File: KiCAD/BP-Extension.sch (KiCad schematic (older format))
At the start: 8 parts, among them P1 CONN_01X06, P2 CONN_01X01, SW1 SW_Push, U1 BP, U2 RFM69

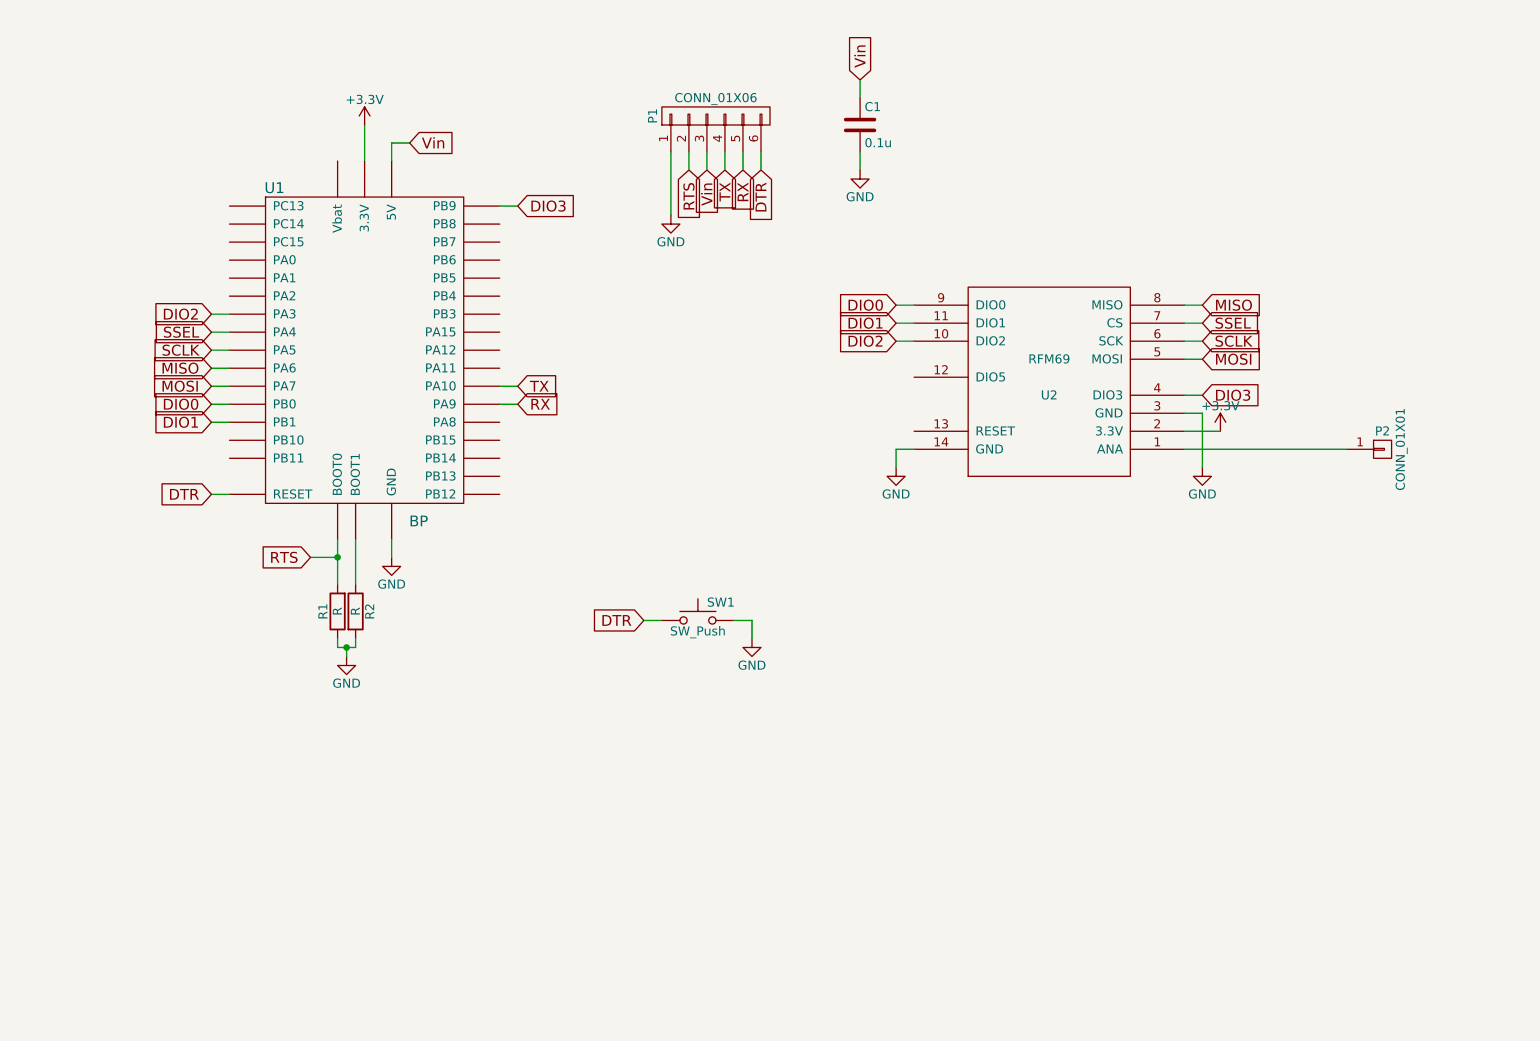
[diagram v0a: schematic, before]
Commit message: Moved 2x03 header to get rid of the offset, #8
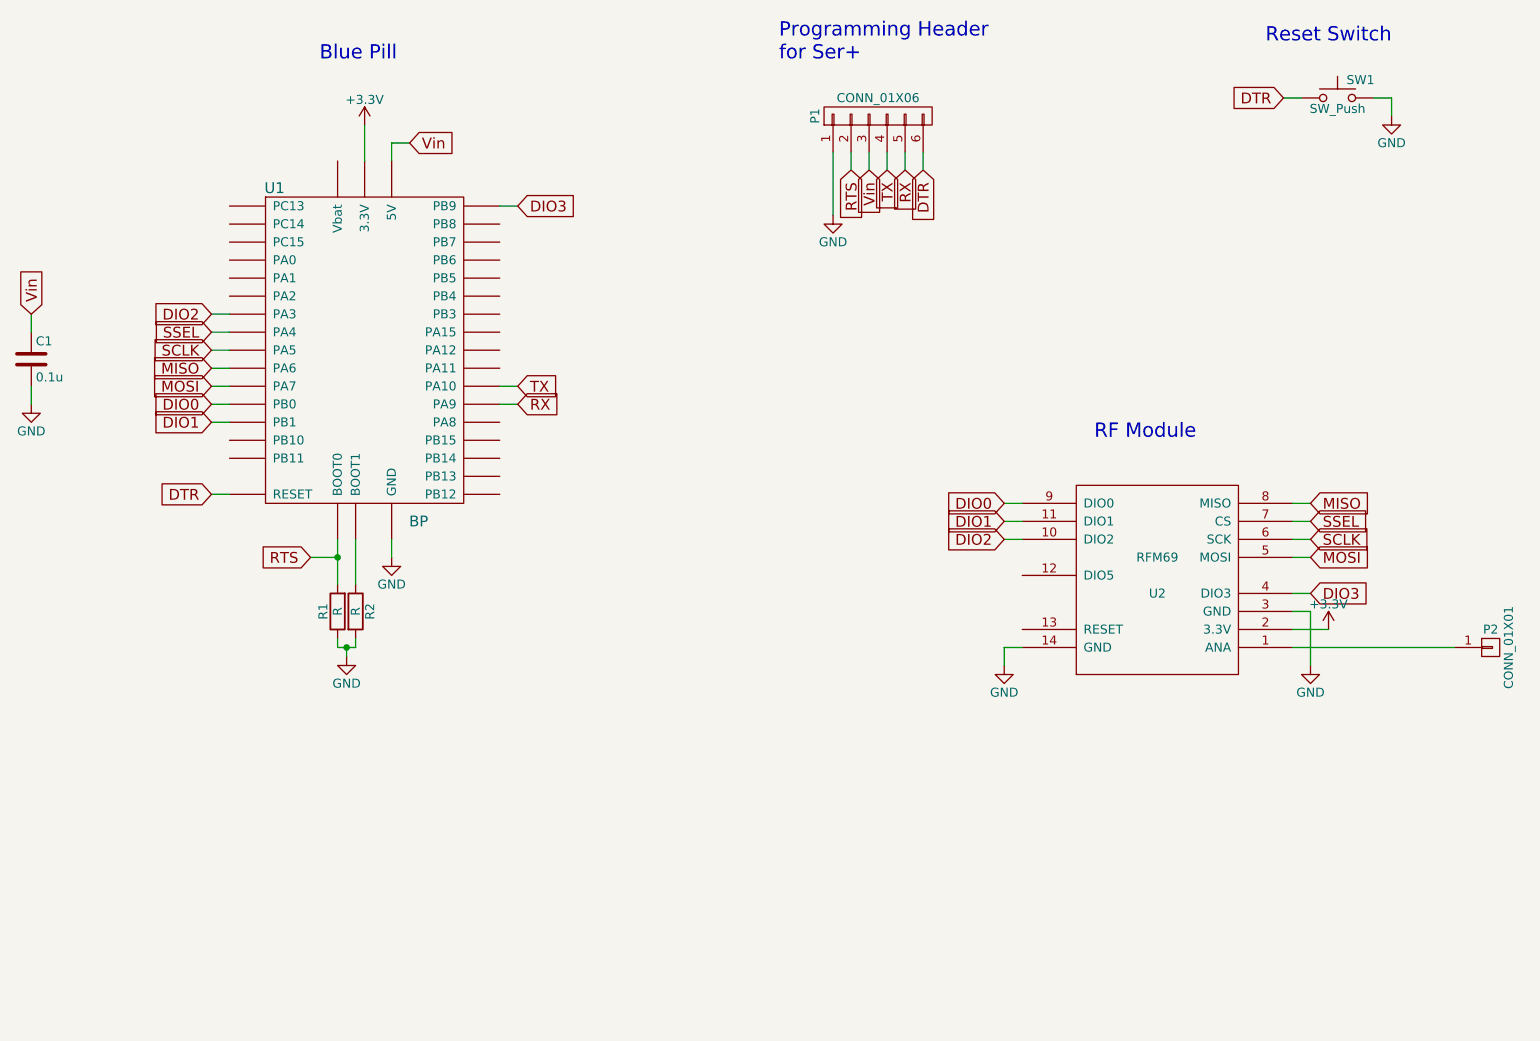
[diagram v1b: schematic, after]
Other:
- note added: "Blue Pill"
- note added: "Programming Header\nfor Ser+"
- note added: "RF Module"
- note added: "Reset Switch"
- moved on the sheet: C1, P1, P2, SW1, U2
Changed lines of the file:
@@
 LIBS:rfm69
 LIBS:switches
-LIBS:mechanical
 LIBS:BP-Extension-cache
 EELAYER 25 0
@@
 L CONN_01X06 P1
 U 1 1 58713DA3
-P 5200 2000
-F 0 "P1" H 5200 2350 50  0000 C CNN
-F 1 "CONN_01X06" V 5300 2000 50  0000 C CNN
-F 2 "Pin_Headers:Pin_Header_Angled_1x06_Pitch2.54mm" H 5200 2000 50  0001 C CNN
-F 3 "" H 5200 2000 50  0000 C CNN
-	1    5200 2000
+P 6100 2000
+F 0 "P1" H 6100 2350 50  0000 C CNN
+F 1 "CONN_01X06" V 6200 2000 50  0000 C CNN
+F 2 "Pin_Headers:Pin_Header_Angled_1x06_Pitch2.54mm" H 6100 2000 50  0001 C CNN
+F 3 "" H 6100 2000 50  0000 C CNN
+	1    6100 2000
 	0    -1   -1   0
 $EndComp
@@
 L GND #PWR04
 U 1 1 58713F1E
-P 4950 2550
-F 0 "#PWR04" H 4950 2300 50  0001 C CNN
-F 1 "GND" H 4950 2400 50  0000 C CNN
-F 2 "" H 4950 2550 50  0000 C CNN
-F 3 "" H 4950 2550 50  0000 C CNN
-	1    4950 2550
-	1    0    0    -1
-$EndComp
-Text GLabel 5050 2300 3    60   Input ~ 0
+P 5850 2550
+F 0 "#PWR04" H 5850 2300 50  0001 C CNN
+F 1 "GND" H 5850 2400 50  0000 C CNN
+F 2 "" H 5850 2550 50  0000 C CNN
+F 3 "" H 5850 2550 50  0000 C CNN
+	1    5850 2550
+	1    0    0    -1
+$EndComp
+Text GLabel 5950 2300 3    60   Input ~ 0
 RTS
-Text GLabel 5250 2300 3    60   Input ~ 0
+Text GLabel 6150 2300 3    60   Input ~ 0
 TX
-Text GLabel 5350 2300 3    60   Input ~ 0
+Text GLabel 6250 2300 3    60   Input ~ 0
 RX
-Text GLabel 5450 2300 3    60   Input ~ 0
+Text GLabel 6350 2300 3    60   Input ~ 0
 DTR
 Text GLabel 2400 4100 0    60   Input ~ 0
@@
 TX
 Wire Wire Line
-	5450 2200 5450 2300
+	6350 2200 6350 2300
 Wire Wire Line
 	2400 4100 2500 4100
@@
 	4000 3600 4100 3600
 Wire Wire Line
-	5250 2300 5250 2200
-Wire Wire Line
-	5350 2200 5350 2300
-Wire Wire Line
-	4950 2200 4950 2550
-Wire Wire Line
-	5050 2200 5050 2300
+	6150 2300 6150 2200
+Wire Wire Line
+	6250 2200 6250 2300
+Wire Wire Line
+	5850 2200 5850 2550
+Wire Wire Line
+	5950 2200 5950 2300
 Text GLabel 2950 4450 0    60   Input ~ 0
 RTS
@@
 	2950 4450 3100 4450
 Connection ~ 3100 4450
-Text GLabel 5150 2300 3    60   Input ~ 0
+Text GLabel 6050 2300 3    60   Input ~ 0
 Vin
 Wire Wire Line
-	5150 2200 5150 2300
+	6050 2200 6050 2300
 Text GLabel 3500 2150 2    60   Input ~ 0
 Vin
@@
 L RFM69 U2
 U 1 1 58716C00
-P 7050 3450
-F 0 "U2" H 7050 3350 50  0000 C CNN
-F 1 "RFM69" H 7050 3550 50  0000 C CNN
-F 2 "RFM69:RFM69CW" H 7050 3050 50  0001 C CNN
-F 3 "DOCUMENTATION" H 7100 2950 50  0001 C CNN
-	1    7050 3450
+P 7650 4550
+F 0 "U2" H 7650 4450 50  0000 C CNN
+F 1 "RFM69" H 7650 4650 50  0000 C CNN
+F 2 "RFM69:RFM69CW" H 7650 4150 50  0001 C CNN
+F 3 "DOCUMENTATION" H 7700 4050 50  0001 C CNN
+	1    7650 4550
 	1    0    0    -1
 $EndComp
@@
 L GND #PWR05
 U 1 1 58716C60
-P 7900 3950
-F 0 "#PWR05" H 7900 3700 50  0001 C CNN
-F 1 "GND" H 7900 3800 50  0000 C CNN
-F 2 "" H 7900 3950 50  0000 C CNN
-F 3 "" H 7900 3950 50  0000 C CNN
-	1    7900 3950
+P 8500 5050
+F 0 "#PWR05" H 8500 4800 50  0001 C CNN
+F 1 "GND" H 8500 4900 50  0000 C CNN
+F 2 "" H 8500 5050 50  0000 C CNN
+F 3 "" H 8500 5050 50  0000 C CNN
+	1    8500 5050
 	1    0    0    -1
 $EndComp
@@
 L +3.3V #PWR06
 U 1 1 58716C96
-P 8000 3750
-F 0 "#PWR06" H 8000 3600 50  0001 C CNN
-F 1 "+3.3V" H 8000 3890 50  0000 C CNN
-F 2 "" H 8000 3750 50  0000 C CNN
-F 3 "" H 8000 3750 50  0000 C CNN
-	1    8000 3750
-	1    0    0    -1
-$EndComp
-Text GLabel 7900 3150 2    60   Input ~ 0
+P 8600 4850
+F 0 "#PWR06" H 8600 4700 50  0001 C CNN
+F 1 "+3.3V" H 8600 4990 50  0000 C CNN
+F 2 "" H 8600 4850 50  0000 C CNN
+F 3 "" H 8600 4850 50  0000 C CNN
+	1    8600 4850
+	1    0    0    -1
+$EndComp
+Text GLabel 8500 4250 2    60   Input ~ 0
 SSEL
-Text GLabel 7900 3250 2    60   Input ~ 0
+Text GLabel 8500 4350 2    60   Input ~ 0
 SCLK
-Text GLabel 7900 3050 2    60   Input ~ 0
+Text GLabel 8500 4150 2    60   Input ~ 0
 MISO
-Text GLabel 7900 3350 2    60   Input ~ 0
+Text GLabel 8500 4450 2    60   Input ~ 0
 MOSI
 $Comp
 L CONN_01X01 P2
 U 1 1 58716DE4
-P 8900 3850
-F 0 "P2" H 8900 3950 50  0000 C CNN
-F 1 "CONN_01X01" V 9000 3850 50  0000 C CNN
-F 2 "Connect:PINTST" H 8900 3850 50  0001 C CNN
-F 3 "" H 8900 3850 50  0000 C CNN
-	1    8900 3850
-	1    0    0    -1
-$EndComp
-Wire Wire Line
-	7800 3650 7900 3650
-Wire Wire Line
-	7900 3650 7900 3950
+P 9500 4950
+F 0 "P2" H 9500 5050 50  0000 C CNN
+F 1 "CONN_01X01" V 9600 4950 50  0000 C CNN
+F 2 "Connect:PINTST" H 9500 4950 50  0001 C CNN
+F 3 "" H 9500 4950 50  0000 C CNN
+	1    9500 4950
+	1    0    0    -1
+$EndComp
+Wire Wire Line
+	8400 4750 8500 4750
+Wire Wire Line
+	8500 4750 8500 5050
 $Comp
 L GND #PWR07
 U 1 1 58717D5A
-P 6200 3950
-F 0 "#PWR07" H 6200 3700 50  0001 C CNN
-F 1 "GND" H 6200 3800 50  0000 C CNN
-F 2 "" H 6200 3950 50  0000 C CNN
-F 3 "" H 6200 3950 50  0000 C CNN
-	1    6200 3950
-	1    0    0    -1
-$EndComp
-Wire Wire Line
-	6300 3850 6200 3850
-Wire Wire Line
-	6200 3850 6200 3950
-Wire Wire Line
-	7800 3750 8000 3750
-Wire Wire Line
-	7800 3050 7900 3050
-Wire Wire Line
-	7900 3150 7800 3150
-Wire Wire Line
-	7800 3250 7900 3250
-Wire Wire Line
-	7900 3350 7800 3350
-Wire Wire Line
-	7800 3850 8700 3850
+P 6800 5050
+F 0 "#PWR07" H 6800 4800 50  0001 C CNN
+F 1 "GND" H 6800 4900 50  0000 C CNN
+F 2 "" H 6800 5050 50  0000 C CNN
+F 3 "" H 6800 5050 50  0000 C CNN
+	1    6800 5050
+	1    0    0    -1
+$EndComp
+Wire Wire Line
+	6900 4950 6800 4950
+Wire Wire Line
+	6800 4950 6800 5050
+Wire Wire Line
+	8400 4850 8600 4850
+Wire Wire Line
+	8400 4150 8500 4150
+Wire Wire Line
+	8500 4250 8400 4250
+Wire Wire Line
+	8400 4350 8500 4350
+Wire Wire Line
+	8500 4450 8400 4450
+Wire Wire Line
+	8400 4950 9300 4950
 Text GLabel 2400 3500 0    60   Input ~ 0
 MOSI
@@
 L SW_Push SW1
 U 1 1 5872565A
-P 5100 4800
-F 0 "SW1" H 5150 4900 50  0000 L CNN
-F 1 "SW_Push" H 5100 4740 50  0000 C CNN
-F 2 "Buttons_Switches_SMD:SW_SPST_EVQP2" H 5100 5000 50  0001 C CNN
-F 3 "" H 5100 5000 50  0000 C CNN
-	1    5100 4800
+P 8650 1900
+F 0 "SW1" H 8700 2000 50  0000 L CNN
+F 1 "SW_Push" H 8650 1840 50  0000 C CNN
+F 2 "Buttons_Switches_SMD:SW_SPST_EVQP2" H 8650 2100 50  0001 C CNN
+F 3 "" H 8650 2100 50  0000 C CNN
+	1    8650 1900
 	1    0    0    -1
 $EndComp
@@
 L GND #PWR08
 U 1 1 587256A4
-P 5400 4900
-F 0 "#PWR08" H 5400 4650 50  0001 C CNN
-F 1 "GND" H 5400 4750 50  0000 C CNN
-F 2 "" H 5400 4900 50  0000 C CNN
-F 3 "" H 5400 4900 50  0000 C CNN
-	1    5400 4900
-	1    0    0    -1
-$EndComp
-Text GLabel 4800 4800 0    60   Input ~ 0
+P 8950 2000
+F 0 "#PWR08" H 8950 1750 50  0001 C CNN
+F 1 "GND" H 8950 1850 50  0000 C CNN
+F 2 "" H 8950 2000 50  0000 C CNN
+F 3 "" H 8950 2000 50  0000 C CNN
+	1    8950 2000
+	1    0    0    -1
+$EndComp
+Text GLabel 8350 1900 0    60   Input ~ 0
 DTR
 Wire Wire Line
-	4800 4800 4900 4800
-Wire Wire Line
-	5300 4800 5400 4800
-Wire Wire Line
-	5400 4800 5400 4900
-Text GLabel 6200 3050 0    60   Input ~ 0
+	8350 1900 8450 1900
+Wire Wire Line
+	8850 1900 8950 1900
+Wire Wire Line
+	8950 1900 8950 2000
+Text GLabel 6800 4150 0    60   Input ~ 0
 DIO0
-Text GLabel 6200 3150 0    60   Input ~ 0
+Text GLabel 6800 4250 0    60   Input ~ 0
 DIO1
-Text GLabel 6200 3250 0    60   Input ~ 0
+Text GLabel 6800 4350 0    60   Input ~ 0
 DIO2
-Text GLabel 7900 3550 2    60   Input ~ 0
+Text GLabel 8500 4650 2    60   Input ~ 0
 DIO3
 Wire Wire Line
-	7900 3550 7800 3550
-Wire Wire Line
-	6200 3250 6300 3250
-Wire Wire Line
-	6300 3150 6200 3150
-Wire Wire Line
-	6200 3050 6300 3050
+	8500 4650 8400 4650
+Wire Wire Line
+	6800 4350 6900 4350
+Wire Wire Line
+	6900 4250 6800 4250
+Wire Wire Line
+	6800 4150 6900 4150
 Text GLabel 2400 3600 0    60   Input ~ 0
 DIO0
@@
 L C C1
 U 1 1 58728A59
-P 6000 2050
-F 0 "C1" H 6025 2150 50  0000 L CNN
-F 1 "0.1u" H 6025 1950 50  0000 L CNN
-F 2 "Capacitors_SMD:C_1206_HandSoldering" H 6038 1900 50  0001 C CNN
-F 3 "" H 6000 2050 50  0000 C CNN
-	1    6000 2050
-	1    0    0    -1
-$EndComp
-Text GLabel 6000 1800 1    60   Input ~ 0
+P 1400 3350
+F 0 "C1" H 1425 3450 50  0000 L CNN
+F 1 "0.1u" H 1425 3250 50  0000 L CNN
+F 2 "Capacitors_SMD:C_1206_HandSoldering" H 1438 3200 50  0001 C CNN
+F 3 "" H 1400 3350 50  0000 C CNN
+	1    1400 3350
+	1    0    0    -1
+$EndComp
+Text GLabel 1400 3100 1    60   Input ~ 0
 Vin
 $Comp
 L GND #PWR09
 U 1 1 58728B32
-P 6000 2300
-F 0 "#PWR09" H 6000 2050 50  0001 C CNN
-F 1 "GND" H 6000 2150 50  0000 C CNN
-F 2 "" H 6000 2300 50  0000 C CNN
-F 3 "" H 6000 2300 50  0000 C CNN
-	1    6000 2300
-	1    0    0    -1
-$EndComp
-Wire Wire Line
-	6000 2300 6000 2200
-Wire Wire Line
-	6000 1900 6000 1800
+P 1400 3600
+F 0 "#PWR09" H 1400 3350 50  0001 C CNN
+F 1 "GND" H 1400 3450 50  0000 C CNN
+F 2 "" H 1400 3600 50  0000 C CNN
+F 3 "" H 1400 3600 50  0000 C CNN
+	1    1400 3600
+	1    0    0    -1
+$EndComp
+Wire Wire Line
+	1400 3600 1400 3500
+Wire Wire Line
+	1400 3200 1400 3100
 Text GLabel 4100 2500 2    60   Input ~ 0
 DIO3
 Wire Wire Line
 	4100 2500 4000 2500
+Text Notes 7300 3800 0    79   ~ 0
+RF Module
+Text Notes 8250 1600 0    79   ~ 0
+Reset Switch
+Text Notes 5550 1700 0    79   ~ 0
+Programming Header\nfor Ser+
+Text Notes 3000 1700 0    79   ~ 0
+Blue Pill
 $EndSCHEMATC

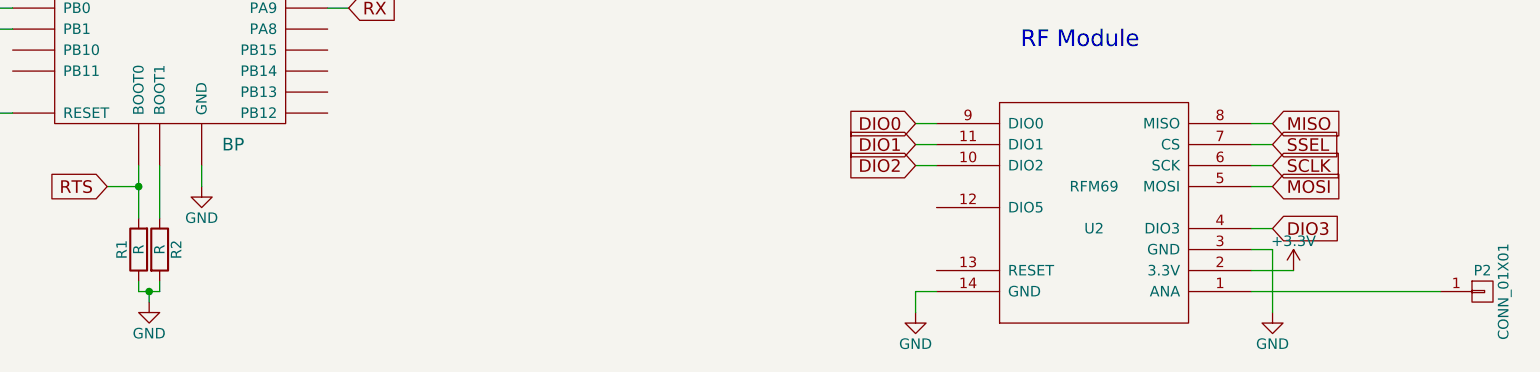
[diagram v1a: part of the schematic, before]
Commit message: Almost ready for rev2. fixes #9, fixes #8, fixes #1
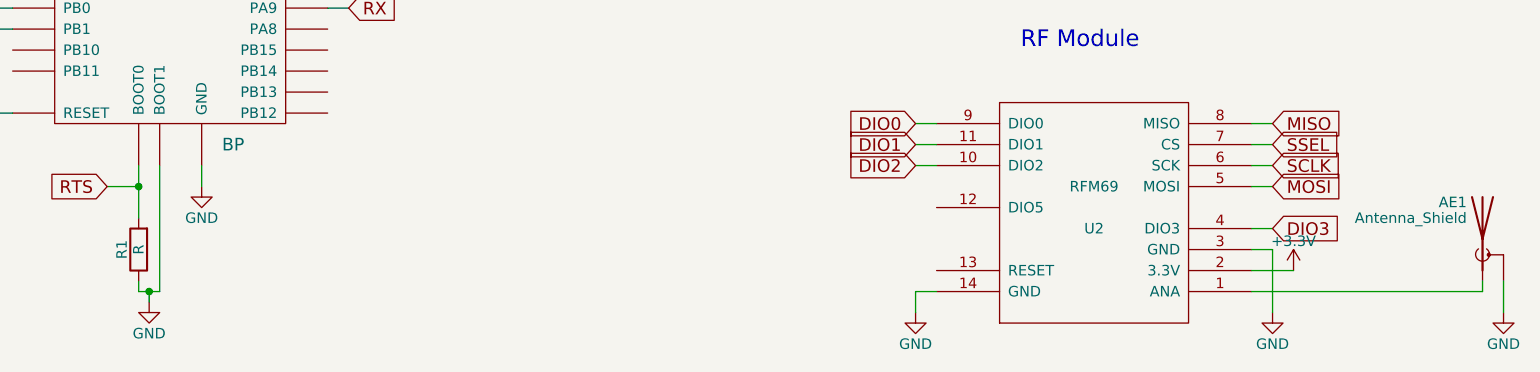
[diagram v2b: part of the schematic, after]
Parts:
- removed P2: CONN_01X01, Connect:PINTST, symbol CONN_01X01
- removed R2: R, Resistors_SMD:R_1206_HandSoldering, symbol R
- added AE1: Antenna_Shield, BP:U.FL-COAX, symbol Antenna_Shield
- C1: footprint Capacitors_SMD:C_1206_HandSoldering -> Capacitors_SMD:C_0805_HandSoldering
- P1: footprint Pin_Headers:Pin_Header_Angled_1x06_Pitch2.54mm -> BP:Pin_Header_Angled_1x06_Pitch2.54mm
- R1: footprint Resistors_SMD:R_1206_HandSoldering -> Resistors_SMD:R_0805_HandSoldering
- SW1: footprint Buttons_Switches_SMD:SW_SPST_EVQP2 -> BP:SMD_BUTTON
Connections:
- net GND: now also U1.PB2 (BOOT1), AE1.2 (Shield)
- net at U2.1 (ANA): now also AE1.1 (A)
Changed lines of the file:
@@
 LIBS:rfm69
 LIBS:switches
+LIBS:mechanical
 LIBS:BP-Extension-cache
 EELAYER 25 0
@@
 F 0 "R1" V 3180 4750 50  0000 C CNN
 F 1 "R" V 3100 4750 50  0000 C CNN
-F 2 "Resistors_SMD:R_1206_HandSoldering" V 3030 4750 50  0001 C CNN
+F 2 "Resistors_SMD:R_0805_HandSoldering" V 3030 4750 50  0001 C CNN
 F 3 "" H 3100 4750 50  0000 C CNN
 	1    3100 4750
 	-1   0    0    1
 $EndComp
-$Comp
-L R R2
-U 1 1 58713C3E
-P 3200 4750
-F 0 "R2" V 3280 4750 50  0000 C CNN
-F 1 "R" V 3200 4750 50  0000 C CNN
-F 2 "Resistors_SMD:R_1206_HandSoldering" V 3130 4750 50  0001 C CNN
-F 3 "" H 3200 4750 50  0000 C CNN
-	1    3200 4750
-	1    0    0    -1
-$EndComp
 Wire Wire Line
 	3100 4350 3100 4600
 Wire Wire Line
-	3200 4600 3200 4350
+	3200 4950 3200 4350
 $Comp
 L GND #PWR01
@@
 Wire Wire Line
 	3150 4950 3150 5000
-Wire Wire Line
-	3200 4950 3200 4900
 Connection ~ 3150 4950
 $Comp
@@
 F 0 "P1" H 6100 2350 50  0000 C CNN
 F 1 "CONN_01X06" V 6200 2000 50  0000 C CNN
-F 2 "Pin_Headers:Pin_Header_Angled_1x06_Pitch2.54mm" H 6100 2000 50  0001 C CNN
+F 2 "BP:Pin_Header_Angled_1x06_Pitch2.54mm" H 6100 2000 50  0001 C CNN
 F 3 "" H 6100 2000 50  0000 C CNN
 	1    6100 2000
@@
 Text GLabel 8500 4450 2    60   Input ~ 0
 MOSI
-$Comp
-L CONN_01X01 P2
-U 1 1 58716DE4
-P 9500 4950
-F 0 "P2" H 9500 5050 50  0000 C CNN
-F 1 "CONN_01X01" V 9600 4950 50  0000 C CNN
-F 2 "Connect:PINTST" H 9500 4950 50  0001 C CNN
-F 3 "" H 9500 4950 50  0000 C CNN
-	1    9500 4950
-	1    0    0    -1
-$EndComp
 Wire Wire Line
 	8400 4750 8500 4750
@@
 	8500 4450 8400 4450
 Wire Wire Line
-	8400 4950 9300 4950
+	8400 4950 9500 4950
 Text GLabel 2400 3500 0    60   Input ~ 0
 MOSI
@@
 F 0 "SW1" H 8700 2000 50  0000 L CNN
 F 1 "SW_Push" H 8650 1840 50  0000 C CNN
-F 2 "Buttons_Switches_SMD:SW_SPST_EVQP2" H 8650 2100 50  0001 C CNN
+F 2 "BP:SMD_BUTTON" H 8650 2100 50  0001 C CNN
 F 3 "" H 8650 2100 50  0000 C CNN
 	1    8650 1900
@@
 F 0 "C1" H 1425 3450 50  0000 L CNN
 F 1 "0.1u" H 1425 3250 50  0000 L CNN
-F 2 "Capacitors_SMD:C_1206_HandSoldering" H 1438 3200 50  0001 C CNN
+F 2 "Capacitors_SMD:C_0805_HandSoldering" H 1438 3200 50  0001 C CNN
 F 3 "" H 1400 3350 50  0000 C CNN
 	1    1400 3350
@@
 Text Notes 3000 1700 0    79   ~ 0
 Blue Pill
+$Comp
+L Antenna_Shield AE1
+U 1 1 589F6A9F
+P 9500 4700
+F 0 "AE1" H 9425 4875 50  0000 R CNN
+F 1 "Antenna_Shield" H 9425 4800 50  0000 R CNN
+F 2 "BP:U.FL-COAX" H 9500 4800 50  0001 C CNN
+F 3 "" H 9500 4800 50  0001 C CNN
+	1    9500 4700
+	1    0    0    -1
+$EndComp
+Wire Wire Line
+	9500 4950 9500 4900
+$Comp
+L GND #PWR010
+U 1 1 589F6D6F
+P 9600 5050
+F 0 "#PWR010" H 9600 4800 50  0001 C CNN
+F 1 "GND" H 9600 4900 50  0000 C CNN
+F 2 "" H 9600 5050 50  0000 C CNN
+F 3 "" H 9600 5050 50  0000 C CNN
+	1    9600 5050
+	1    0    0    -1
+$EndComp
+Wire Wire Line
+	9600 5050 9600 4900
 $EndSCHEMATC
